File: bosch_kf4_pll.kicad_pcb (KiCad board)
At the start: 2 copper layers, 17.8 x 31.1 mm, 15 parts, among them J1 AVR-ISP-6, J2 CPD18U42CD, Q1 Q_NPN_BEC, U1 ATmega328P-AU, U2 AMS1117-5.0

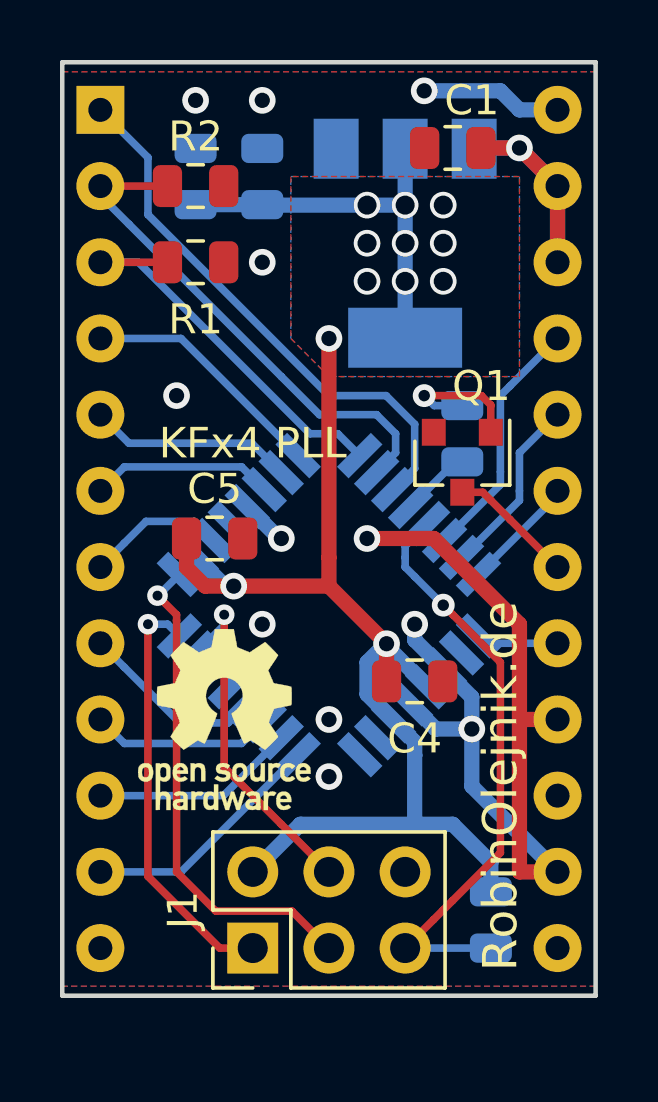
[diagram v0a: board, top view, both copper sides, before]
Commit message: Updated schematic and pcb to new version.
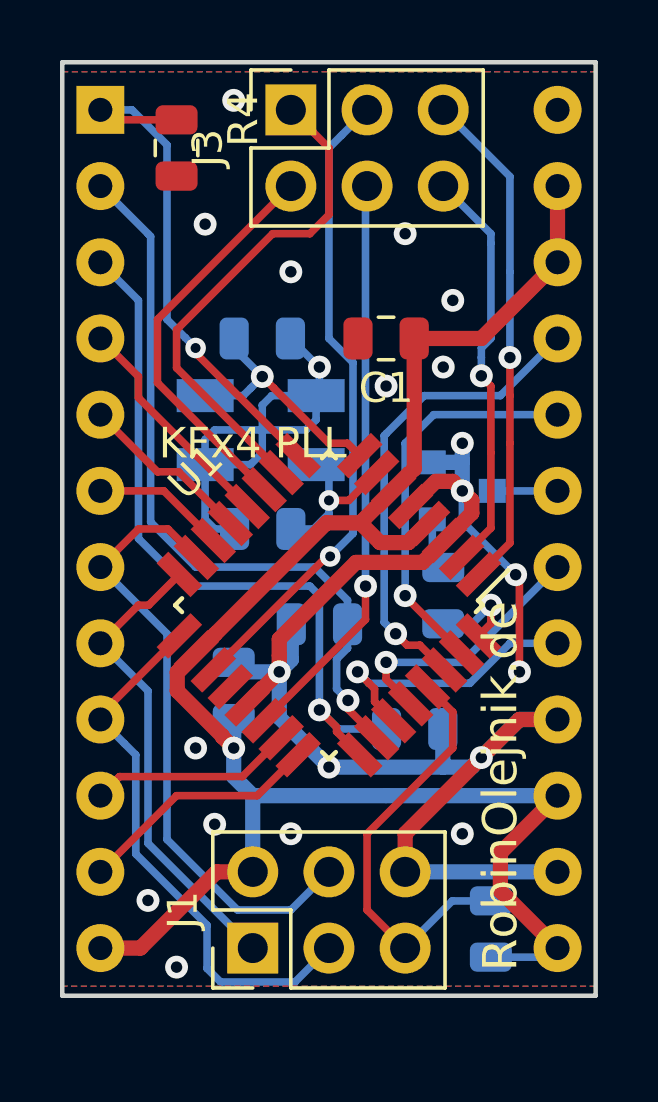
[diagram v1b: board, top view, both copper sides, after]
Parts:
- removed C5: 100n, Capacitor_SMD:C_0805_2012Metric
- removed REF**: OSHW-Logo_5.7x6mm_SilkScreen, Symbol:OSHW-Logo_5.7x6mm_SilkScreen
- removed U2: AMS1117-5.0, Package_TO_SOT_SMD:SOT-223-3_TabPin2
- added J3: ACC, Connector_PinSocket_2.54mm:PinSocket_2x03_P2.54mm_Vertical, F.Cu at (132.1, 62.2)
- added R5: 47k, Resistor_SMD:R_0805_2012Metric, B.Cu at (137.2, 78.4)
- added Y1: 20M, Crystal:Crystal_SMD_EuroQuartz_MJ-4Pin_5.0x3.2mm, B.Cu at (131.1, 72.9)
- C1: value 100n -> 10u
- C2: value 10u -> 100n
- C3: value 100n -> 12p
- C4: value 100n -> 12p; moved to B.Cu
- Q1, R2: moved to B.Cu
- R1: value 47k -> 10k; moved to B.Cu
- R3: value 10k -> 47k
- R4, U1: moved to F.Cu
- moved R1 24.3 mm to (138.7, 89.5), turned to 90 degrees
- moved R2 19.5 mm to (136.2, 82.9)
- moved C2 17.2 mm to (130.2, 81.6)
- moved R4 13.5 mm to (128.3, 63.5)
- moved C4 12.5 mm to (131.1, 69.8), turned to 180 degrees
- moved C3 12.0 mm to (131.1, 76.2), turned to 0 degrees
- moved R3 11.4 mm to (133.0, 79.4), turned to 180 degrees
- moved C1 6.73 mm to (135.3, 69.8)
- moved Q1 0.95 mm to (137.8, 74.9), turned to 0 degrees
- turned U1 to 225 degrees
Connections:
- C1 pad 1: +8V -> +5V
- C3 pad 1: +5V -> GND
- C3 pad 2: GND -> Net-(C3-Pad2)
- C4 pad 1: +5V -> GND
- C4 pad 2: GND -> Net-(C4-Pad2)
- J1 pad 1: MISO -> D4
- J1 pad 3: SCK -> D5
- J1 pad 4: MOSI -> D3
- J2 pad 1: A -> SQL
- J2 pad 12: Net-(J2-Pad12) -> +5V
- J2 pad 13: Net-(J2-Pad13) -> +5V
- J2 pad 15: Net-(J2-Pad15) -> +5V
- J2 pad 18: PTT_OUT -> A
- J2 pad 19: SQL -> PTT_OUT
- J2 pad 22: +8V -> +5V
- J2 pad 23: +8V -> +5V
- R1 pad 1: A0 -> +5V
- R1 pad 2: GND -> RST
- R2 pad 1: A1 -> A0
- R3 pad 1: +5V -> A1
- R3 pad 2: RST -> GND
- R4 pad 1: Net-(Q1-Pad1) -> SQL
- R4 pad 2: PTT -> GND
- U1 pad 1: PTT_SENSE -> GPIO_A
- U1 pad 10: D6 -> PWM_A
- U1 pad 11: D5 -> PWM_B
- U1 pad 12: D4 -> D0
- U1 pad 13: PWM_A -> D1
- U1 pad 14: PWM_B -> D2
- U1 pad 15: MOSI -> D3
- U1 pad 16: MISO -> D4
- U1 pad 17: SCK -> D5
- U1 pad 19: D3 -> ADC_A
- U1 pad 2: Net-(U1-Pad2) -> GPIO_B
- U1 pad 22: D2 -> ADC_B
- U1 pad 23: D1 -> D6
- U1 pad 24: D0 -> D7
- U1 pad 27: A -> PTT_SENSE
- U1 pad 28: PTT -> A
- U1 pad 32: SQL -> PTT
- U1 pad 7: Net-(U1-Pad7) -> Net-(C3-Pad2)
- U1 pad 8: Net-(U1-Pad8) -> Net-(C4-Pad2)
- U1 pad 9: D7 -> SQL
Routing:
- net GND: track 36.0 -> 70.2 mm, vias 12 -> 21
- net ADC_A: track 0.00 -> 21.5 mm, vias 0 -> 1
- net ADC_B: track 0.00 -> 19.2 mm, vias 0 -> 1
- net PWM_A: track 0.00 -> 16.9 mm
- net GPIO_A: track 0.00 -> 16.8 mm, vias 0 -> 1
- net SCK: track 16.6 -> 0.00 mm, vias 1 -> 0
- net D3: track 4.66 -> 21.0 mm
- net MISO: track 14.1 -> 0.00 mm, vias 1 -> 0
- net GPIO_B: track 0.00 -> 13.7 mm, vias 0 -> 1
- net SQL: track 3.88 -> 17.6 mm, vias 0 -> 1
- net PWM_B: track 0.00 -> 13.4 mm
- net D5: track 6.11 -> 18.4 mm
- net MOSI: track 11.7 -> 0.00 mm, vias 1 -> 0
- net A0: track 13.6 -> 25.1 mm, vias 0 -> 1
- net +8V: track 11.5 -> 0.00 mm, vias 1 -> 0
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- removed copper zone on B.Cu, net +5V
- removed copper zone on F.Cu, net +5V
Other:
- net class power added: clearance 0.1524, trace_width 0.508, via_dia 0.6858, via_drill 0.3302

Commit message: Removed last DRC errors
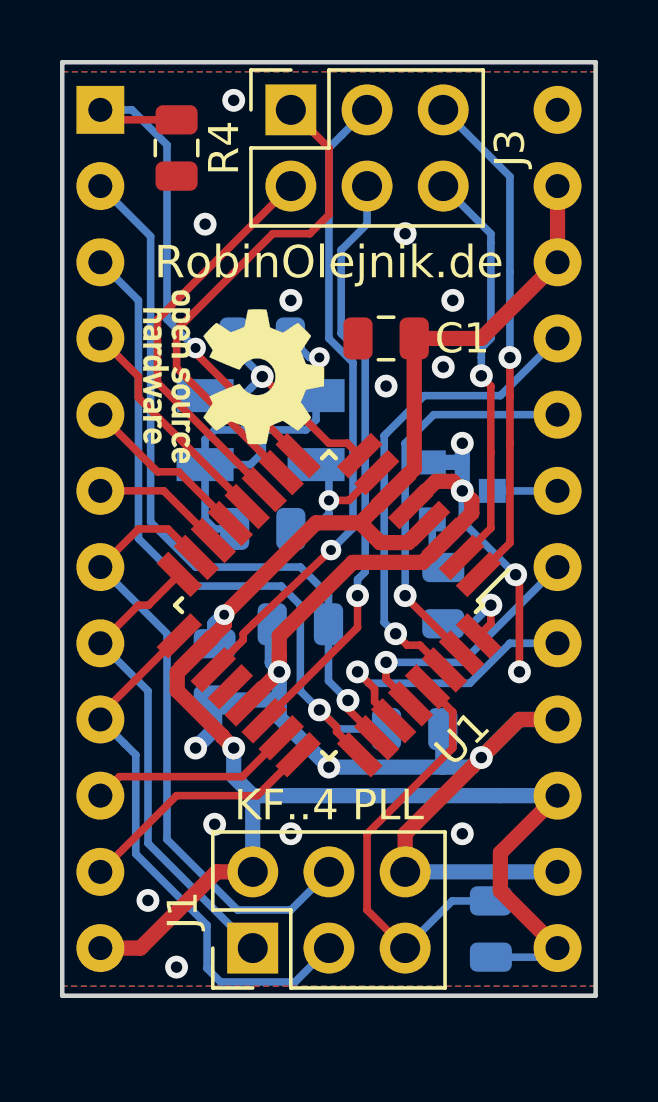
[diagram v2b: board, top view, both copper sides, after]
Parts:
- added REF**: OSHW-Logo_5.7x6mm_SilkScreen, Symbol:OSHW-Logo_5.7x6mm_SilkScreen, F.Cu at (130.2, 71.1)
- moved C2 0.89 mm to (129.5, 81.0), turned to 270 degrees
- moved R3 0.63 mm to (132.4, 79.4)
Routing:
- net GND: track 70.2 -> 72.4 mm
- net ADC_B: track 19.2 -> 20.0 mm
- net A1: track 24.8 -> 24.3 mm
- net A0: track 25.1 -> 24.5 mm
- net +5V: track 60.3 -> 60.6 mm, vias 1 -> 2
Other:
- board text added: "KF..4 PLL"
- board text removed: "KFx4 PLL"

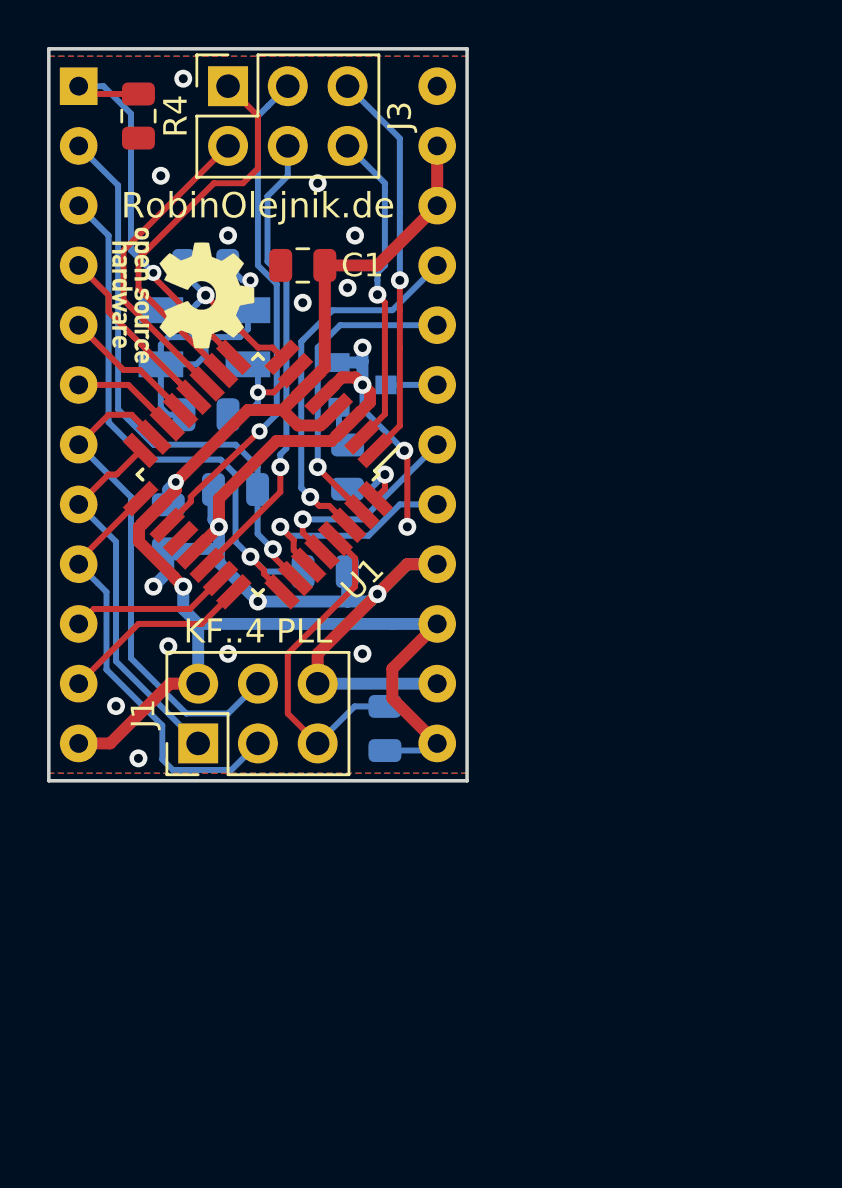
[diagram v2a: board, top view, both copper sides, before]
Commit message: PCB remake with WCH CH32V003 controller
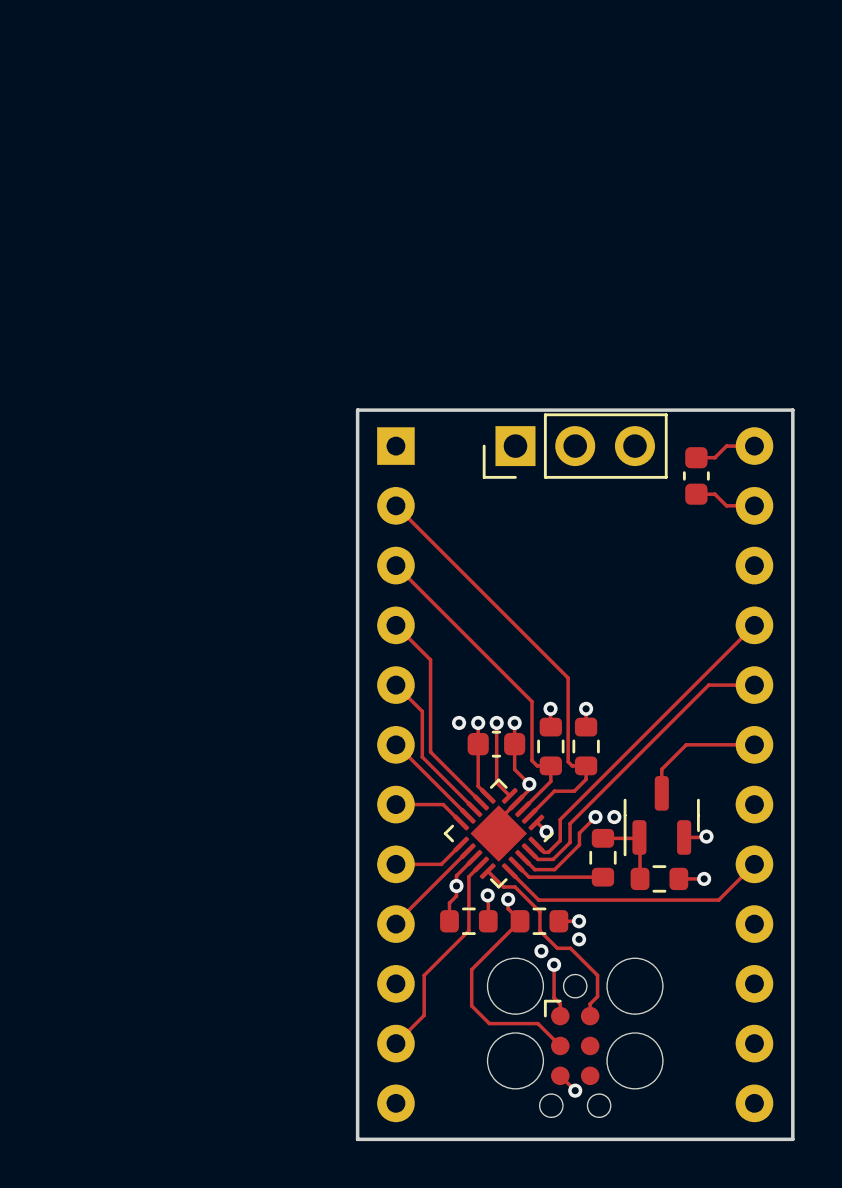
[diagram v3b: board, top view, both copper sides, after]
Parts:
- removed C3, C4: 12p, Capacitor_SMD:C_0805_2012Metric
- removed J3: ACC, Connector_PinSocket_2.54mm:PinSocket_2x03_P2.54mm_Vertical
- removed REF**: OSHW-Logo_5.7x6mm_SilkScreen, Symbol:OSHW-Logo_5.7x6mm_SilkScreen
- removed Y1: 20M, Crystal:Crystal_SMD_EuroQuartz_MJ-4Pin_5.0x3.2mm
- added J4: audio, Connector_PinHeader_2.54mm:PinHeader_1x03_P2.54mm_Vertical, F.Cu at (144.3, 77.5)
- added R6: 47k, Resistor_SMD:R_0603_1608Metric, F.Cu at (150.4, 95.9)
- C1: value 10u -> 100n; footprint Capacitor_SMD:C_0805_2012Metric -> Capacitor_SMD:C_0603_1608Metric
- C2: value 100n -> 10u; footprint Capacitor_SMD:C_0805_2012Metric -> Capacitor_SMD:C_0603_1608Metric; moved to F.Cu
- J1: value AVR-ISP-6 -> Conn_ARM_SWD_TagConnect_TC2030-NL; footprint Connector_PinHeader_2.54mm:PinHeader_2x03_P2.54mm_Vertical -> Connector:Tag-Connect_TC2030-IDC-FP_2x03_P1.27mm_Vertical
- Q1: value Q_NPN_BEC -> AO3400A; moved to F.Cu
- R1: value 10k -> 47k; footprint Resistor_SMD:R_0805_2012Metric -> Resistor_SMD:R_0603_1608Metric; moved to F.Cu
- R2, R3, R5: footprint Resistor_SMD:R_0805_2012Metric -> Resistor_SMD:R_0603_1608Metric; moved to F.Cu
- R4: footprint Resistor_SMD:R_0805_2012Metric -> Resistor_SMD:R_0603_1608Metric
- U1: value ATmega328P-AU -> CH32V003F4U6; footprint Package_QFP:TQFP-32_7x7mm_P0.8mm -> Package_DFN_QFN:WQFN-20-1EP_3x3mm_P0.4mm_EP1.7x1.7mm
- moved R4 37.0 mm to (142.3, 97.7), turned to 0 degrees
- moved C2 22.6 mm to (152.0, 78.8), turned to 90 degrees
- moved Q1 22.3 mm to (150.5, 93.2), turned to 90 degrees
- moved C1 22.0 mm to (143.5, 90.2), turned to 0 degrees
- moved J1 20.5 mm to (146.8, 103.0), turned to -90 degrees
- moved J2 20.4 mm to (139.2, 77.5)
- moved R5 19.8 mm to (148.0, 95.0), turned to 90 degrees
- moved R3 18.5 mm to (147.3, 90.3), turned to 90 degrees
- moved U1 18.4 mm to (143.6, 94.0)
- moved R2 12.1 mm to (145.8, 90.3), turned to 90 degrees
- moved R1 10.5 mm to (145.3, 97.7), turned to 180 degrees
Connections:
- J1 pad 1: D4 -> +5V
- J1 pad 2: +5V -> SWIO
- J1 pad 3: D5 -> RESET
- J1 pad 4: D3 -> unconnected-(J1-SWCLK-Pad4)
- J1 pad 5: RST -> GND
- J1 pad 6: GND -> unconnected-(J1-SWO-Pad6)
- J2 pad 10: D6 -> unconnected-(J2-Pin_10-Pad10)
- J2 pad 18: A -> unconnected-(J2-Pin_18-Pad18)
- Q1 pad 1: Net-(Q1-Pad1) -> Net-(Q1-G)
- R1 pad 2: RST -> RESET
- R5 pad 1: Net-(Q1-Pad1) -> PTT
- R5 pad 2: PTT -> Net-(Q1-G)
- U1 pad 1: GPIO_A -> RESET
- U1 pad 10: PWM_A -> D3
- U1 pad 11: PWM_B -> D4
- U1 pad 12: D0 -> D5
- U1 pad 13: D1 -> SQL
- U1 pad 14: D2 -> D7
- U1 pad 15: D3 -> SWIO
- U1 pad 16: D4 -> PTT_SENSE
- U1 pad 17: D5 -> PTT
- U1 pad 18: +5V -> ADC
- U1 pad 19: ADC_A -> TXD
- U1 pad 2: GPIO_B -> A1
- U1 pad 20: Net-(U1-Pad20) -> RXD
- U1 pad 3: GND -> A0
- U1 pad 4: +5V -> GND
- U1 pad 5: GND -> DAC
- U1 pad 7: Net-(C3-Pad2) -> D0
- U1 pad 8: Net-(C4-Pad2) -> D1
- U1 pad 9: SQL -> D2
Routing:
- net GND: track 72.4 -> 13.8 mm, vias 21 -> 12
- net +5V: track 60.6 -> 9.09 mm, vias 2 -> 3
- net ADC_A: track 21.6 -> 0.00 mm, vias 1 -> 0
- net ADC: track 0.00 -> 20.9 mm, vias 0 -> 1
- net ADC_B: track 20.0 -> 0.00 mm, vias 1 -> 0
- net D3: track 21.0 -> 3.09 mm
- net PWM_A: track 16.9 -> 0.00 mm
- net GPIO_A: track 16.8 -> 0.00 mm, vias 1 -> 0
- net DAC: track 0.00 -> 15.4 mm, vias 0 -> 1
- net RST: track 14.3 -> 0.00 mm
- net RESET: track 0.00 -> 14.2 mm, vias 0 -> 2
- net D5: track 18.4 -> 4.36 mm
- net GPIO_B: track 13.7 -> 0.00 mm, vias 1 -> 0
- net PWM_B: track 13.4 -> 0.00 mm
- net D4: track 15.8 -> 3.12 mm
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- added copper zone on In2.Cu, net +5V
- added copper zone on In1.Cu, net GND
- removed copper zone on F.Cu, net GND
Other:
- board size 17.8 x 31.1 mm -> 18.5 x 31 mm
- copper layers 2 -> 4
- net class Default removed
- net class power removed
- rule pad_to_mask_clearance: 0.0508 -> 0
- board text removed: "KF..4 PLL"
- board text removed: "RobinOlejnik.de"

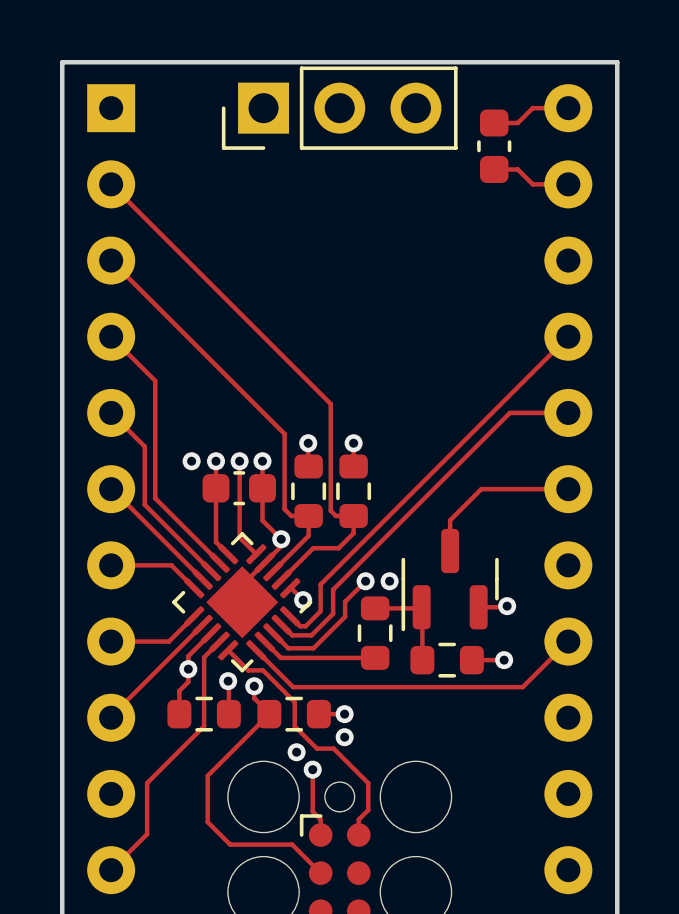
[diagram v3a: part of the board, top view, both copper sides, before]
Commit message: Added CTCSS filters
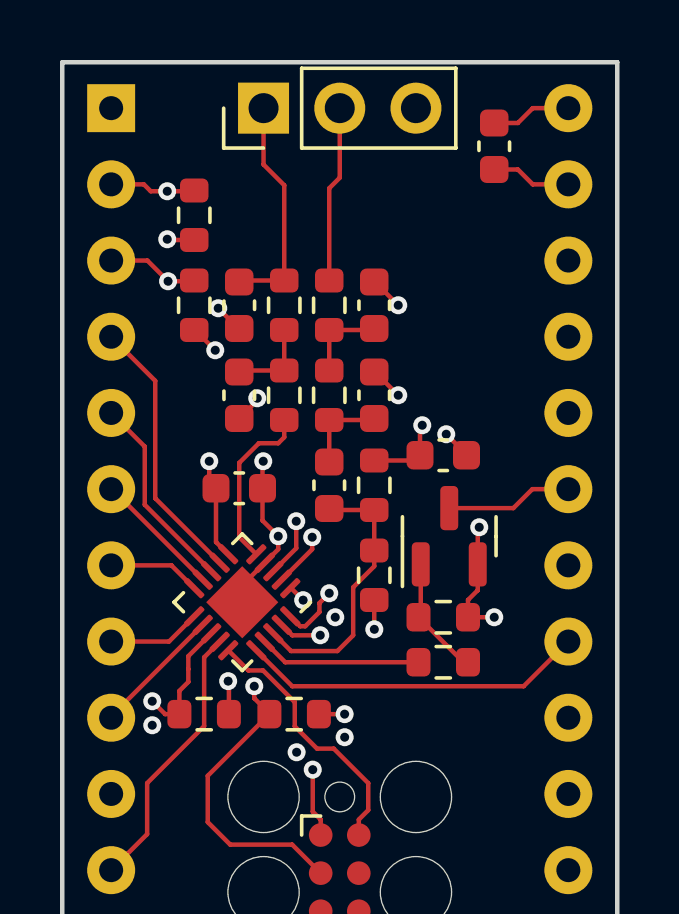
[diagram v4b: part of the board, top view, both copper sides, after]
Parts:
- added C3: 10u, Capacitor_SMD:C_0603_1608Metric, F.Cu at (146.5, 90.1)
- added C4: 100n, Capacitor_SMD:C_0603_1608Metric, F.Cu at (148.0, 87.1)
- added C5: 100n, Capacitor_SMD:C_0603_1608Metric, F.Cu at (148.0, 84.1)
- added C6: 100n, Capacitor_SMD:C_0603_1608Metric, F.Cu at (143.5, 87.1)
- added C7: 100n, Capacitor_SMD:C_0603_1608Metric, F.Cu at (143.5, 84.1)
- added C8: 100n, Capacitor_SMD:C_0603_1608Metric, F.Cu at (150.3, 89.1)
- added R10: 47k, Resistor_SMD:R_0603_1608Metric, F.Cu at (146.5, 84.1)
- added R11: 47k, Resistor_SMD:R_0603_1608Metric, F.Cu at (145.0, 87.1)
- added R12: 47k, Resistor_SMD:R_0603_1608Metric, F.Cu at (145.0, 84.1)
- added R7: 47k, Resistor_SMD:R_0603_1608Metric, F.Cu at (148.0, 90.1)
- added R8: 47k, Resistor_SMD:R_0603_1608Metric, F.Cu at (148.0, 93.1)
- added R9: 47k, Resistor_SMD:R_0603_1608Metric, F.Cu at (146.5, 87.1)
- J1: value Conn_ARM_SWD_TagConnect_TC2030-NL -> PROG
- moved R3 10.6 mm to (142.0, 81.1), turned to -90 degrees
- moved R2 7.28 mm to (142.0, 84.1), turned to -90 degrees
- moved R5 2.47 mm to (150.3, 96.0), turned to 0 degrees
- moved R6 1.44 mm to (150.3, 94.5)
- moved Q1 1.43 mm to (150.5, 91.8)
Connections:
- J4 pad 1: DAC -> CTCSS_OUT
- J4 pad 2: ADC -> CTCSS_IN
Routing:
- net +5V: track 9.09 -> 46.7 mm, vias 3 -> 4
- net ADC: track 20.9 -> 9.12 mm, vias 1 -> 0
- net DAC: track 15.4 -> 5.71 mm, vias 1 -> 0
- net GND: track 13.8 -> 22.1 mm, vias 12 -> 18
- net CTCSS_OUT: track 0.00 -> 7.61 mm
- net CTCSS_IN: track 0.00 -> 5.89 mm
- net Net-(C3-Pad1): track 0.00 -> 2.92 mm
- net Net-(C6-Pad1): track 0.00 -> 2.87 mm
- net Net-(C5-Pad1): track 0.00 -> 2.87 mm
- net A0: track 13.9 -> 16.2 mm, vias 0 -> 2
- net SQL: track 22.9 -> 24.6 mm
- net PTT: track 3.90 -> 5.41 mm
- net A1: track 18.4 -> 19.7 mm, vias 0 -> 2
- net PTT_OUT: track 5.39 -> 4.23 mm
- net RXD: track 13.9 -> 14.8 mm, vias 0 -> 1
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
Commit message: Finalized Rev2, added gerbers and PDF schematic
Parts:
- added kibuzzard-655EAB0A: G***, kibuzzard-655EAB0A, F.Cu at (152.1, 101.8)
- added kibuzzard-655EABBF: G***, kibuzzard-655EABBF, F.Cu at (149.4, 80.7)
- added kibuzzard-655EABCC: G***, kibuzzard-655EABCC, F.Cu at (146.8, 80.7)
- added kibuzzard-655EABEF: G***, kibuzzard-655EABEF, F.Cu at (144.3, 80.7)
- moved J4 5.06 mm to (149.4, 77.5), turned to -90 degrees
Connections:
- J4 pad 1: CTCSS_OUT -> GND
- J4 pad 3: GND -> CTCSS_OUT
